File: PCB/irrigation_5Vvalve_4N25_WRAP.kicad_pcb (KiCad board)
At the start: 6 copper layers, 13 parts, among them J1 Batt, J2 Sol, J3 Valve, J4 Soil sensor, Q1 TIP120, SW1 ON/OFF, U3 WeMos_mini, U6 TP4056

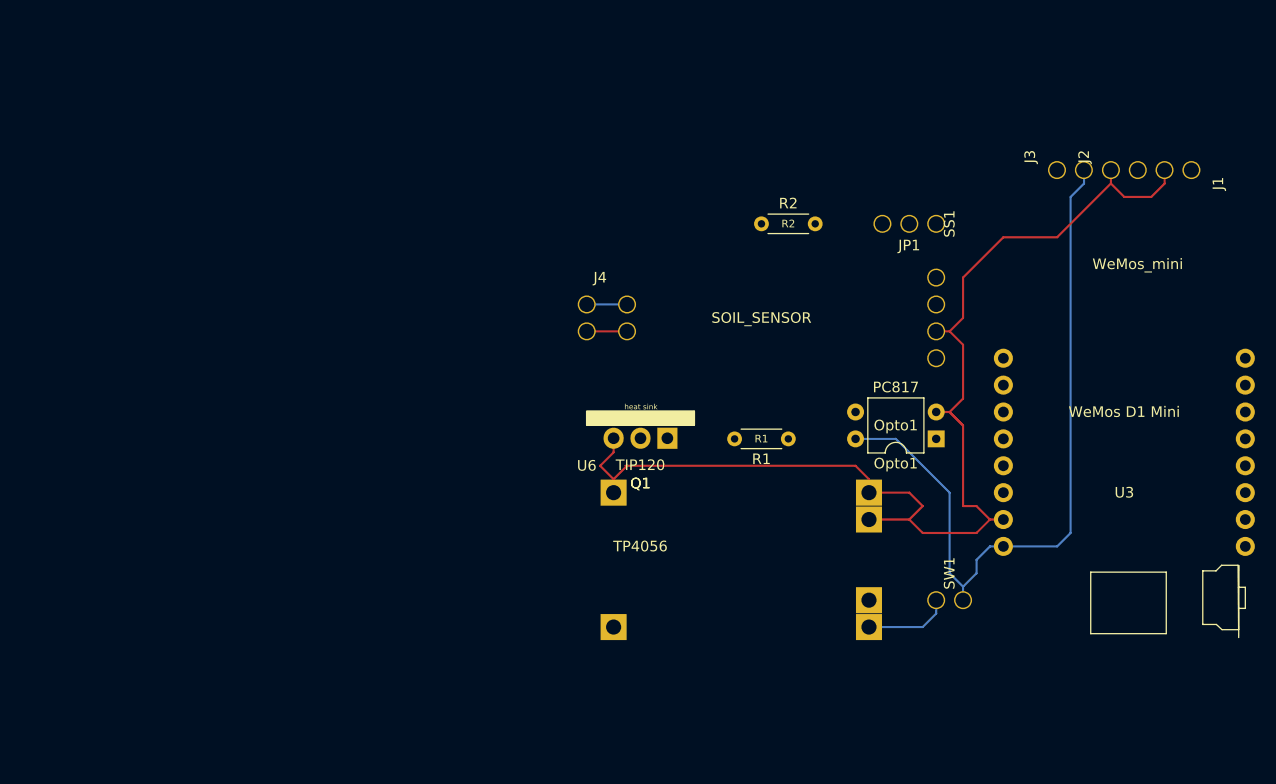
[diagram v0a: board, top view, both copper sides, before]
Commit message: - Changed DeepSleep handling. - Modified Firebase parameters handling Deep Sleep - Added time adjustment to danish summertime (permanently). - Added power down of sensor unit during setup() - Changed schematics and wrap layout of hardware - added some loose power calculations of solar charging - some general clean-up (non functional)
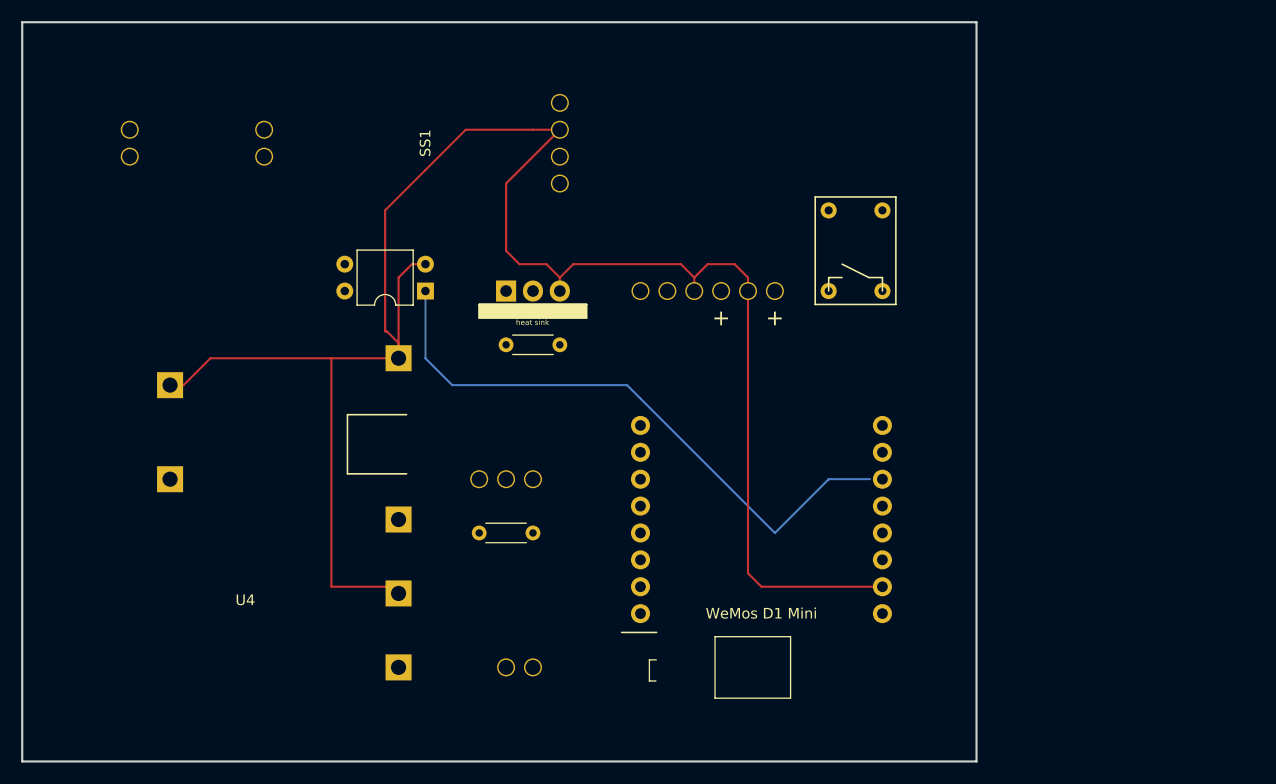
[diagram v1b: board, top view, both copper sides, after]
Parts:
- removed U3: WeMos_mini, wemos_d1_mini:D1_mini_board_v4
- removed U6: TP4056, footprint:TP4056_v4
- added SW2: flash, footprint:pushbutton 3x4 pin, F.Cu at (81.3, 35.6)
- added U2: WeMos_mini, wemos_d1_mini:D1_mini_board_v9, F.Cu at (94.0, 81.3)
- added U4: J5019, footprint:J5019_v3, F.Cu at (55.9, 81.3)
- J1: value Batt -> Sol
- J2: value Sol -> Batt
- R1: value 5k -> 100k
- R2: value 100k -> 5k
- SS1: footprint footprint:Soil sensor_v3 -> footprint:Soil sensor_v5
- moved Opto1 50.2 mm to (55.9, 43.2)
- moved J4 46.2 mm to (30.5, 30.5)
- moved JP1 45.1 mm to (63.5, 63.5)
- moved J2 45.0 mm to (81.3, 45.7), turned to 180 degrees
- moved SW1 41.1 mm to (66.0, 76.2)
- moved J3 41.0 mm to (78.7, 40.6)
- moved SS1 39.2 mm to (71.1, 22.9)
- moved J1 37.4 mm to (88.9, 40.6), turned to 0 degrees
- moved R1 25.7 mm to (66.0, 66.0)
- moved R2 22.2 mm to (68.6, 48.3), turned to 180 degrees
- moved Q1 20.6 mm to (63.5, 43.2), turned to 0 degrees
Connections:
- J1 pad 1: Net-(J1-Pad1) -> GND
- J1 pad 2: GND -> Net-(J1-Pad2)
- J2 pad 1: GND -> Net-(J2-Pad1)
- J2 pad 2: Net-(J2-Pad2) -> GND
- R1 pad 1: Net-(R1-Pad1) -> Net-(J2-Pad1)
- R1 pad 2: Net-(Q1-Pad1) -> Net-(JP1-Pad3)
- R2 pad 1: Net-(J1-Pad1) -> Net-(R2-Pad1)
- R2 pad 2: Net-(JP1-Pad3) -> Net-(Q1-Pad1)
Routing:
- net Net-(J2-Pad1): track 0.00 -> 97.4 mm
- net Net-(J2-Pad2): track 96.3 -> 0.00 mm
- net Net-(J1-Pad2): track 0.00 -> 88.2 mm
- net Net-(J1-Pad1): track 88.2 -> 0.00 mm
- net Net-(R1-Pad1): track 86.2 -> 0.00 mm
- net GND: track 111.3 -> 178.8 mm
- net Net-(J3-Pad2): track 69.5 -> 120.9 mm
- net Net-(Opto1-Pad1): track 8.15 -> 57.3 mm
- net Net-(J3-Pad1): track 58.1 -> 16.3 mm
- net Net-(U3-Pad11): track 36.9 -> 0.00 mm
- net Net-(JP1-Pad2): track 53.0 -> 16.6 mm
- net Net-(SW2-Pad1): track 0.00 -> 33.9 mm
- net Net-(JP1-Pad1): track 5.08 -> 35.7 mm
- net Net-(R2-Pad1): track 0.00 -> 29.3 mm
- net Net-(SW2-Pad2): track 0.00 -> 26.8 mm
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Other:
- board outline added: 90.2 x 69.8 mm
- board text removed: "D0"
- board text removed: "D5"
- board text removed: "flash"
